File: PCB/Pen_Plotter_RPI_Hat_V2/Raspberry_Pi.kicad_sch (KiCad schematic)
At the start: 13 parts, among them J7 PAPER_SENSOR, J8 DC_MOTOR, U7 LM393AN

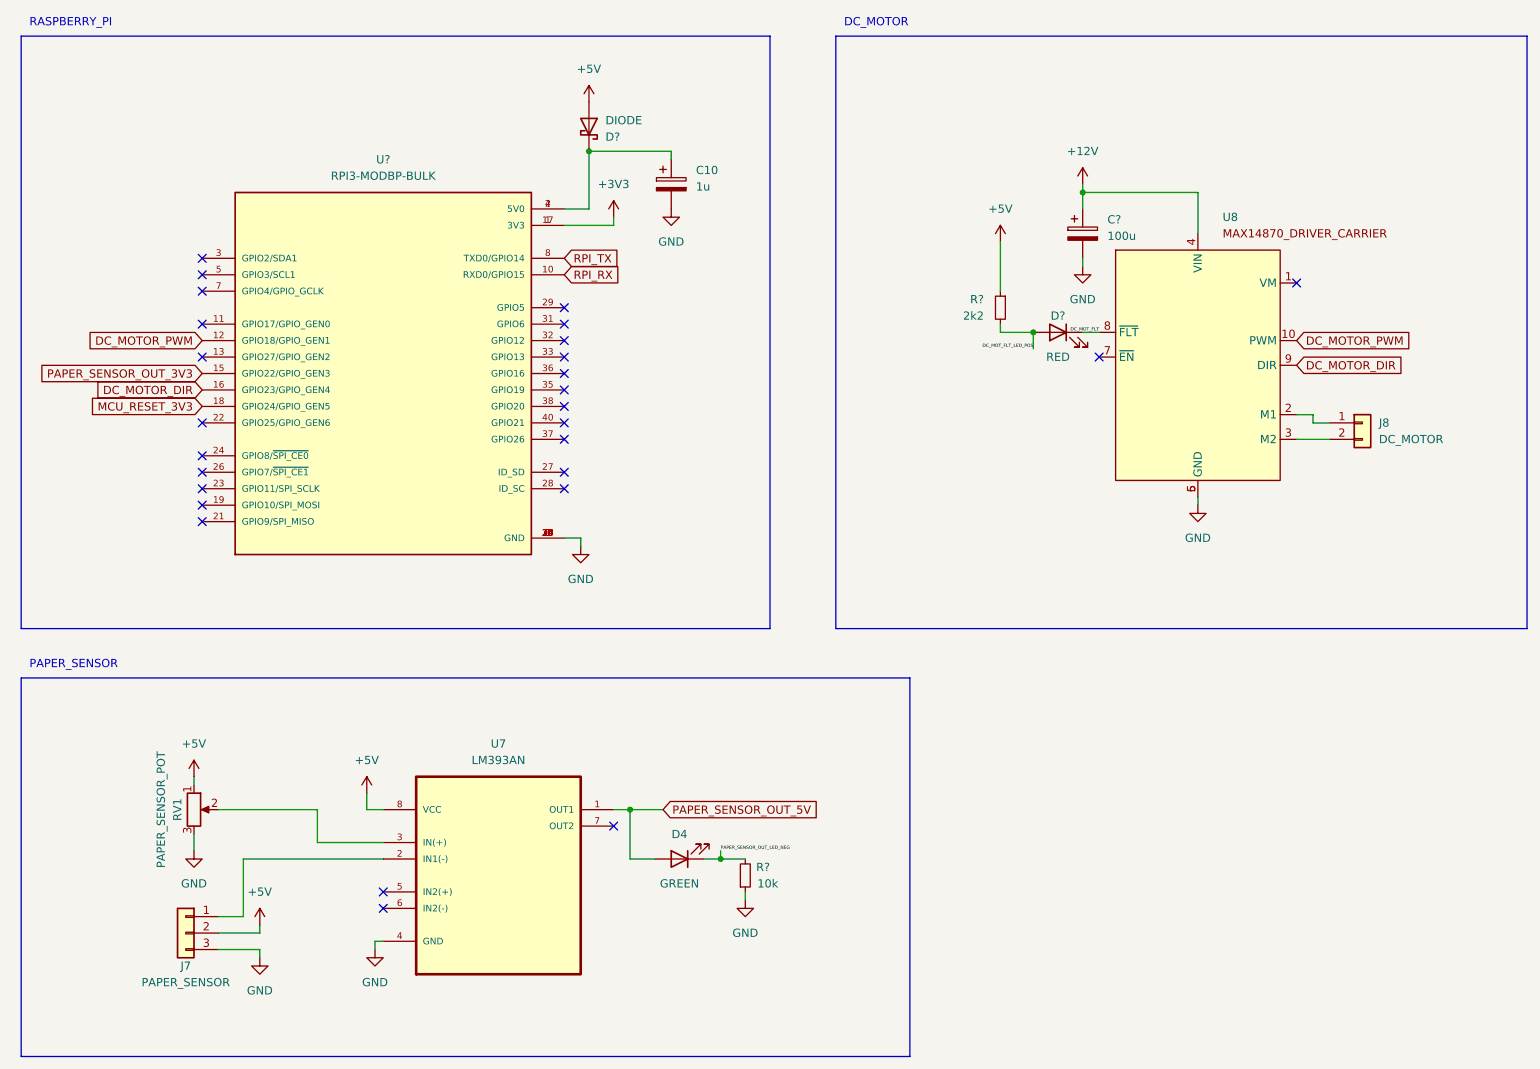
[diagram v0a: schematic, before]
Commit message: Simplified design, began layout process
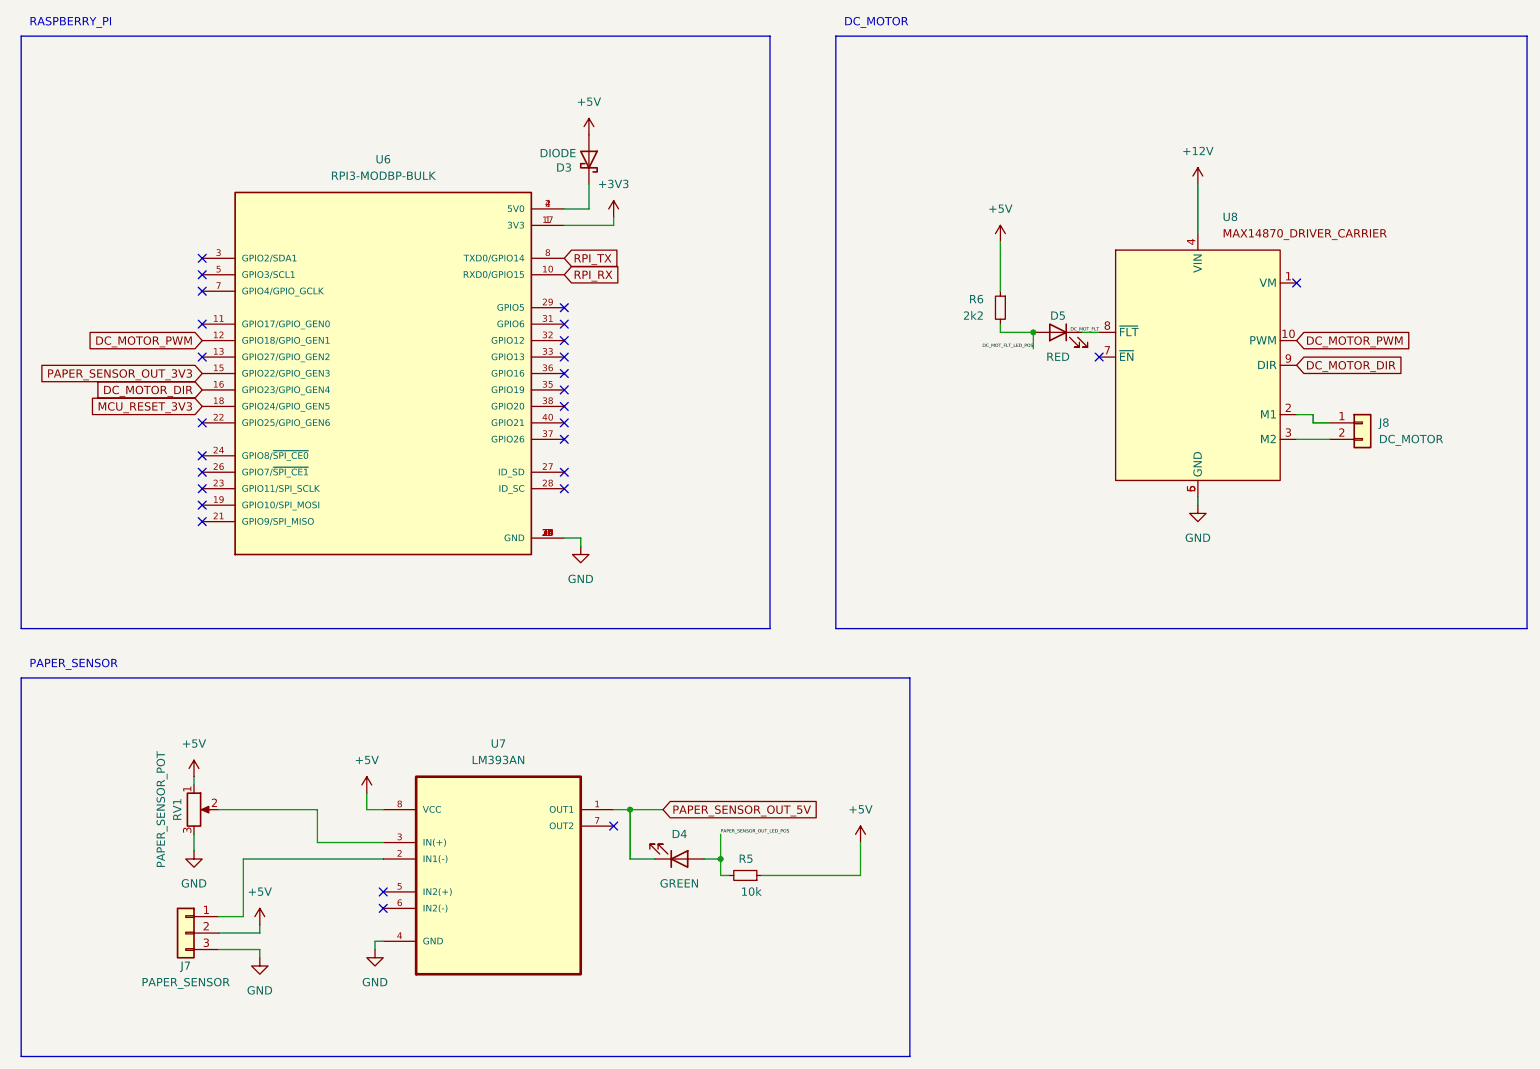
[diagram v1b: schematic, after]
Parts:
- removed C10: 1u, Capacitor_SMD:C_0805_2012Metric, symbol Device:C_Polarized
- removed C?: 100u, Capacitor_SMD:C_1206_3216Metric, symbol Device:C_Polarized
- D3: renamed from D?; footprint Pen_Plotter_Lib:THT_RESISTOR_WITH_VALUE -> Diode_THT:D_5W_P10.16mm_Horizontal
- J7: footprint (none) -> Connector_JST:JST_EH_B3B-EH-A_1x03_P2.50mm_Vertical
- J8: footprint (none) -> Connector_JST:JST_EH_B2B-EH-A_1x02_P2.50mm_Vertical
- gave numbers to parts that had none: 4
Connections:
- net +5V: now also R5.1
- net GND: no longer R5.1
- net PAPER_SENSOR_OUT_5V: now also D4.1 (K); no longer D4.2 (A)
- net PAPER_SENSOR_OUT_LED_NEG renamed PAPER_SENSOR_OUT_LED_POS
- net PAPER_SENSOR_OUT_LED_POS: now also D4.2 (A); no longer D4.1 (K)
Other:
- moved on the sheet: D3, D4, R5

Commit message: Completed PCB component layout, routing and silkscreen work is still needed
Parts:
- RV1: footprint (none) -> Potentiometer_THT:Potentiometer_Bourns_3299W_Vertical
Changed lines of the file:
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@@
       (effects (font (size 1.27 1.27)))
     )
-    (property "Footprint" "" (at 62.23 147.32 0)
+    (property "Footprint" "Potentiometer_THT:Potentiometer_Bourns_3299W_Vertical" (at 62.23 147.32 0)
       (effects (font (size 1.27 1.27)) hide)
     )

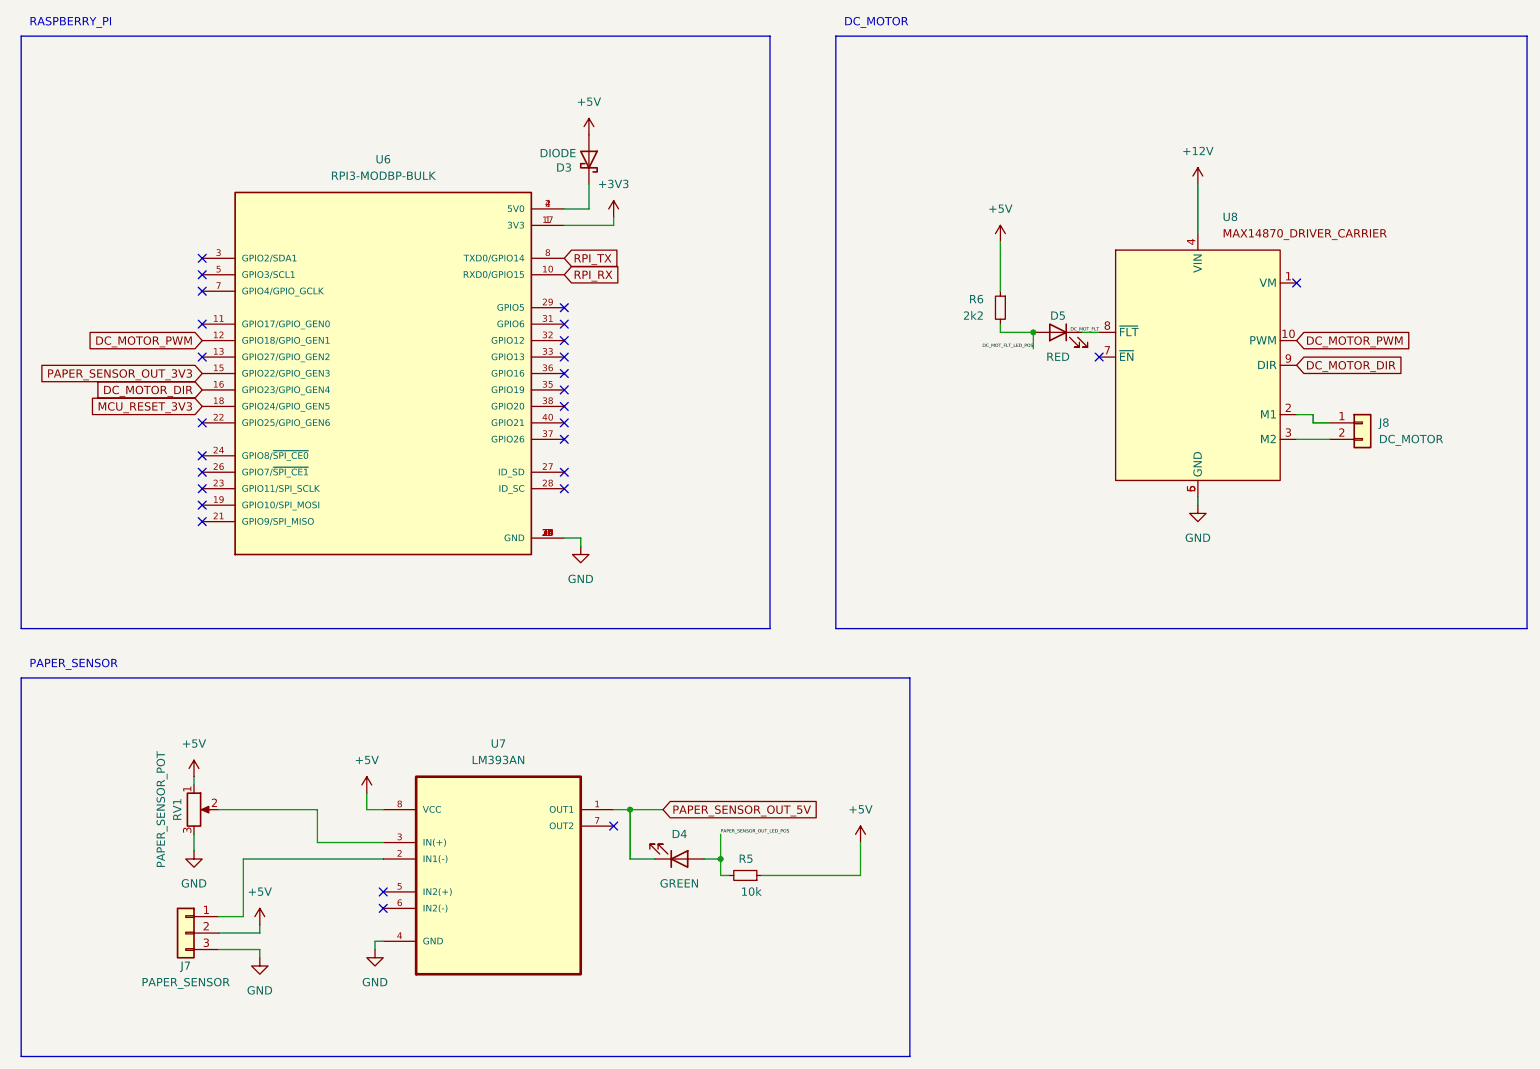
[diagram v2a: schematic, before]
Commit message: Started work on converting to atmega328p control circuit
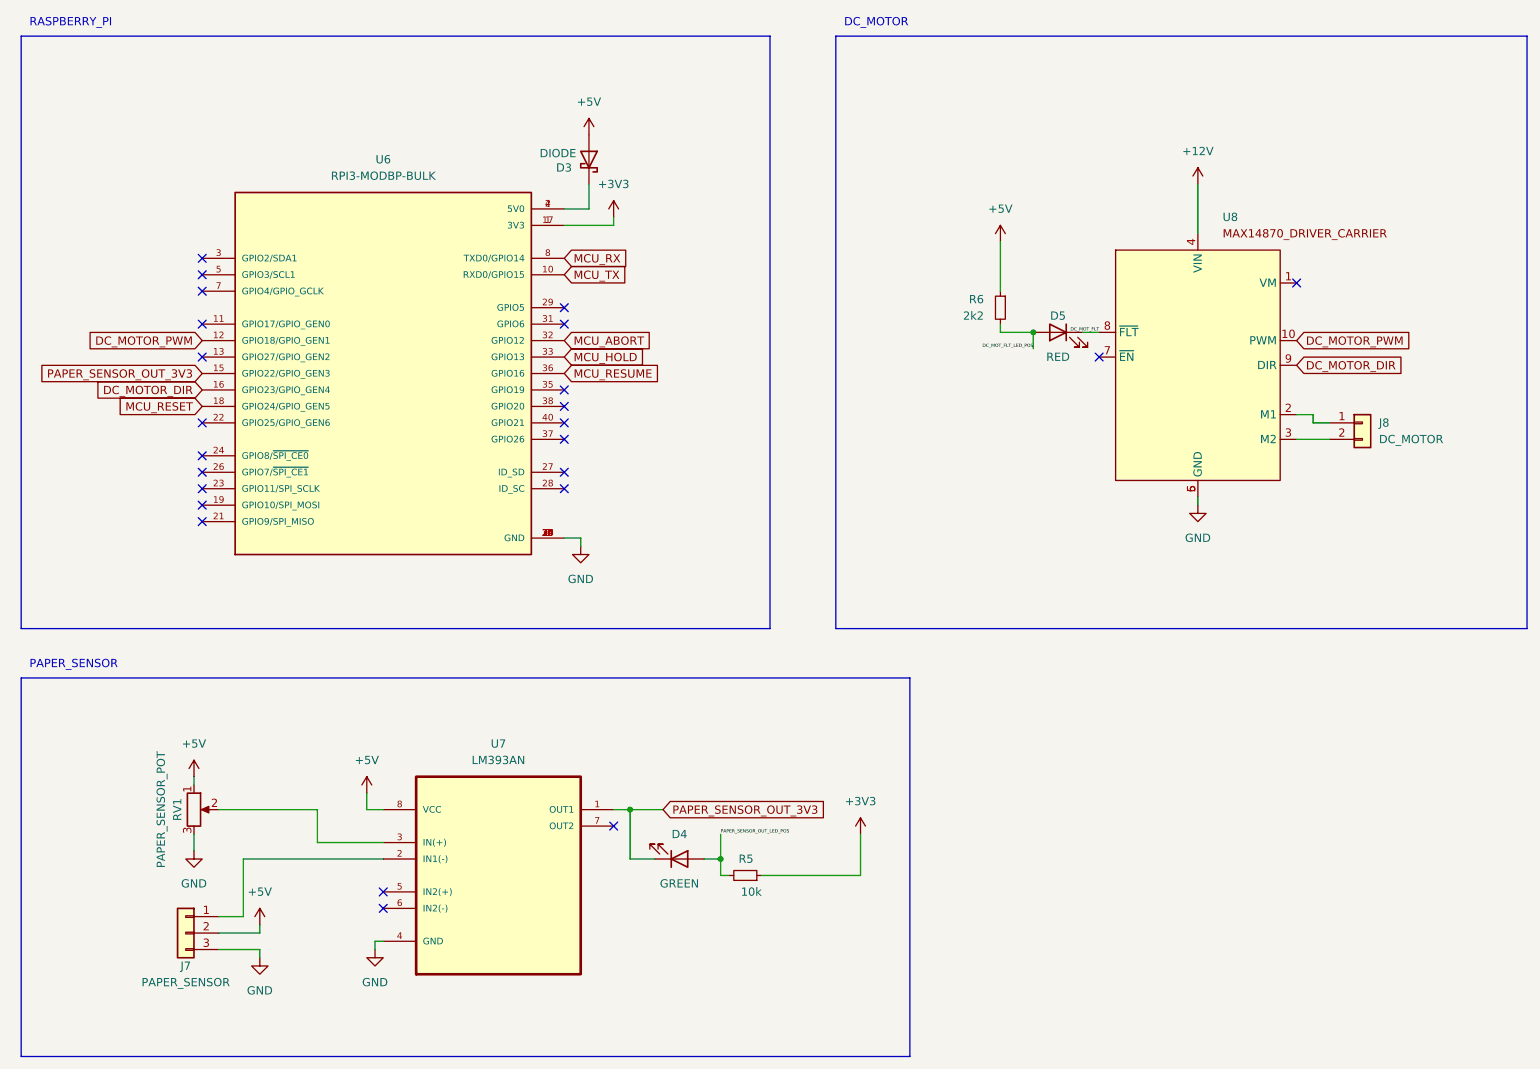
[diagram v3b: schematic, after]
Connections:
- net PAPER_SENSOR_OUT_5V is gone; now on net PAPER_SENSOR_OUT_3V3: D4.1 (K), U7.1 (OUT1)
- net +3V3: now also R5.1
- net +5V: no longer R5.1
- net MCU_ABORT: now reaches U6.32 (GPIO12)
- net MCU_HOLD: now reaches U6.33 (GPIO13)
- net MCU_RESUME: now reaches U6.36 (GPIO16)
- net MCU_RESET_3V3 renamed MCU_RESET
- net RPI_RX renamed MCU_TX
- net RPI_TX renamed MCU_RX
- no-connect marks 27 -> 24
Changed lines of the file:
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@@
   (no_connect (at 63.5 64.77))
   (no_connect (at 91.44 160.02))
-  (no_connect (at 119.38 80.01))
   (no_connect (at 119.38 95.25))
   (no_connect (at 119.38 72.39))
-  (no_connect (at 119.38 77.47))
   (no_connect (at 127 149.86))
   (no_connect (at 63.5 77.47))
@@
   (no_connect (at 119.38 90.17))
   (no_connect (at 63.5 87.63))
-  (no_connect (at 119.38 74.93))
   (no_connect (at 63.5 72.39))
   (wire (pts (xy 69.85 154.94) (xy 91.44 154.94))
@@
     (stroke (width 0) (type default))
   )
-  (wire (pts (xy 165.1 152.4) (xy 165.1 157.48))
+  (wire (pts (xy 165.1 151.13) (xy 165.1 157.48))
     (stroke (width 0) (type default))
   )
@@
     )
   )
-  (global_label "MCU_RESET_3V3" (shape input) (at 63.5 85.09 180) (fields_autoplaced)
-    (effects (font (size 1.27 1.27)) (justify right))
-    (property "Intersheetrefs" "${INTERSHEET_REFS}" (at 45.275 85.09 0)
-      (effects (font (size 1.27 1.27)) (justify right) hide)
+  (global_label "MCU_ABORT" (shape input) (at 119.38 74.93 0) (fields_autoplaced)
+    (effects (font (size 1.27 1.27)) (justify left))
+    (property "Intersheetrefs" "${INTERSHEET_REFS}" (at 133.3114 74.93 0)
+      (effects (font (size 1.27 1.27)) (justify left) hide)
     )
   )
@@
     )
   )
-  (global_label "RPI_RX" (shape input) (at 119.38 64.77 0) (fields_autoplaced)
+  (global_label "MCU_HOLD" (shape input) (at 119.38 77.47 0) (fields_autoplaced)
     (effects (font (size 1.27 1.27)) (justify left))
-    (property "Intersheetrefs" "${INTERSHEET_REFS}" (at 128.9571 64.77 0)
+    (property "Intersheetrefs" "${INTERSHEET_REFS}" (at 132.3438 77.47 0)
       (effects (font (size 1.27 1.27)) (justify left) hide)
+    )
+  )
+  (global_label "MCU_TX" (shape input) (at 119.38 64.77 0) (fields_autoplaced)
+    (effects (font (size 1.27 1.27)) (justify left))
+    (property "Intersheetrefs" "${INTERSHEET_REFS}" (at 129.5618 64.77 0)
+      (effects (font (size 1.27 1.27)) (justify left) hide)
+    )
+  )
+  (global_label "PAPER_SENSOR_OUT_3V3" (shape input) (at 134.62 147.32 0) (fields_autoplaced)
+    (effects (font (size 1.27 1.27)) (justify left))
+    (property "Intersheetrefs" "${INTERSHEET_REFS}" (at 161.1908 147.32 0)
+      (effects (font (size 1.27 1.27)) (justify left) hide)
+    )
+  )
+  (global_label "MCU_RESUME" (shape input) (at 119.38 80.01 0) (fields_autoplaced)
+    (effects (font (size 1.27 1.27)) (justify left))
+    (property "Intersheetrefs" "${INTERSHEET_REFS}" (at 134.9441 80.01 0)
+      (effects (font (size 1.27 1.27)) (justify left) hide)
+    )
+  )
+  (global_label "MCU_RESET" (shape input) (at 63.5 85.09 180) (fields_autoplaced)
+    (effects (font (size 1.27 1.27)) (justify right))
+    (property "Intersheetrefs" "${INTERSHEET_REFS}" (at 49.7502 85.09 0)
+      (effects (font (size 1.27 1.27)) (justify right) hide)
     )
   )
@@
     )
   )
-  (global_label "RPI_TX" (shape input) (at 119.38 62.23 0) (fields_autoplaced)
-    (effects (font (size 1.27 1.27)) (justify left))
-    (property "Intersheetrefs" "${INTERSHEET_REFS}" (at 128.6547 62.23 0)
-      (effects (font (size 1.27 1.27)) (justify left) hide)
-    )
-  )
   (global_label "DC_MOTOR_DIR" (shape input) (at 63.5 82.55 180) (fields_autoplaced)
     (effects (font (size 1.27 1.27)) (justify right))
@@
     )
   )
-  (global_label "PAPER_SENSOR_OUT_5V" (shape input) (at 134.62 147.32 0) (fields_autoplaced)
+  (global_label "MCU_RX" (shape input) (at 119.38 62.23 0) (fields_autoplaced)
     (effects (font (size 1.27 1.27)) (justify left))
-    (property "Intersheetrefs" "${INTERSHEET_REFS}" (at 159.9813 147.32 0)
+    (property "Intersheetrefs" "${INTERSHEET_REFS}" (at 129.8642 62.23 0)
       (effects (font (size 1.27 1.27)) (justify left) hide)
     )
@@
         (path "/a2e71921-3692-4a11-8676-7b25cde44301/9a787dec-5e3d-458a-9d68-7e3e2e8f88b3"
           (reference "U7") (unit 1)
-        )
-      )
-    )
-  )
-  (symbol (lib_id "power:+5V") (at 165.1 152.4 0) (unit 1)
-    (in_bom yes) (on_board yes) (dnp no) (fields_autoplaced)
-    (property "Reference" "#PWR02" (at 165.1 156.21 0)
-      (effects (font (size 1.27 1.27)) hide)
-    )
-    (property "Value" "+5V" (at 165.1 147.32 0)
-      (effects (font (size 1.27 1.27)))
-    )
-    (property "Footprint" "" (at 165.1 152.4 0)
-      (effects (font (size 1.27 1.27)) hide)
-    )
-    (property "Datasheet" "" (at 165.1 152.4 0)
-      (effects (font (size 1.27 1.27)) hide)
-    )
-    (pin "1")
-    (instances
-      (project "Pen_Plotter_RPI_Hat_V2"
-        (path "/a2e71921-3692-4a11-8676-7b25cde44301/9a787dec-5e3d-458a-9d68-7e3e2e8f88b3"
-          (reference "#PWR02") (unit 1)
         )
       )
@@
         )
       )
+    )
+  )
+  (symbol (lib_id "power:+3V3") (at 165.1 151.13 0) (unit 1)
+    (in_bom yes) (on_board yes) (dnp no) (fields_autoplaced)
+    (property "Reference" "#PWR01" (at 165.1 154.94 0)
+      (effects (font (size 1.27 1.27)) hide)
+    )
+    (property "Value" "+3V3" (at 165.1 146.05 0)
+      (effects (font (size 1.27 1.27)))
+    )
+    (property "Footprint" "" (at 165.1 151.13 0)
+      (effects (font (size 1.27 1.27)) hide)
+    )
+    (property "Datasheet" "" (at 165.1 151.13 0)
+      (effects (font (size 1.27 1.27)) hide)
+    )
+    (pin "1")
+    (instances
+      (project "Pen_Plotter_RPI_Hat_V2"
+        (path "/a2e71921-3692-4a11-8676-7b25cde44301/9a787dec-5e3d-458a-9d68-7e3e2e8f88b3"
+          (reference "#PWR01") (unit 1)
+        )
+      )
